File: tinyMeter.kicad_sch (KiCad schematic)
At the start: 30 parts, among them J1 USB_MASTER, J2 DC_POWER, J3 USB_POWER, J4 USBA_OUT_2, J5 USBA_OUT_1, J6 DC_POWER, Q1 BUK9832-55A, Q2 BUK9832-55A, Q3 BUK9832-55A, U1 ESP32-S3, U2 INA219AxD, U3 INA219AxD, U4 INA219AxD, U5 AMS1117-3.3

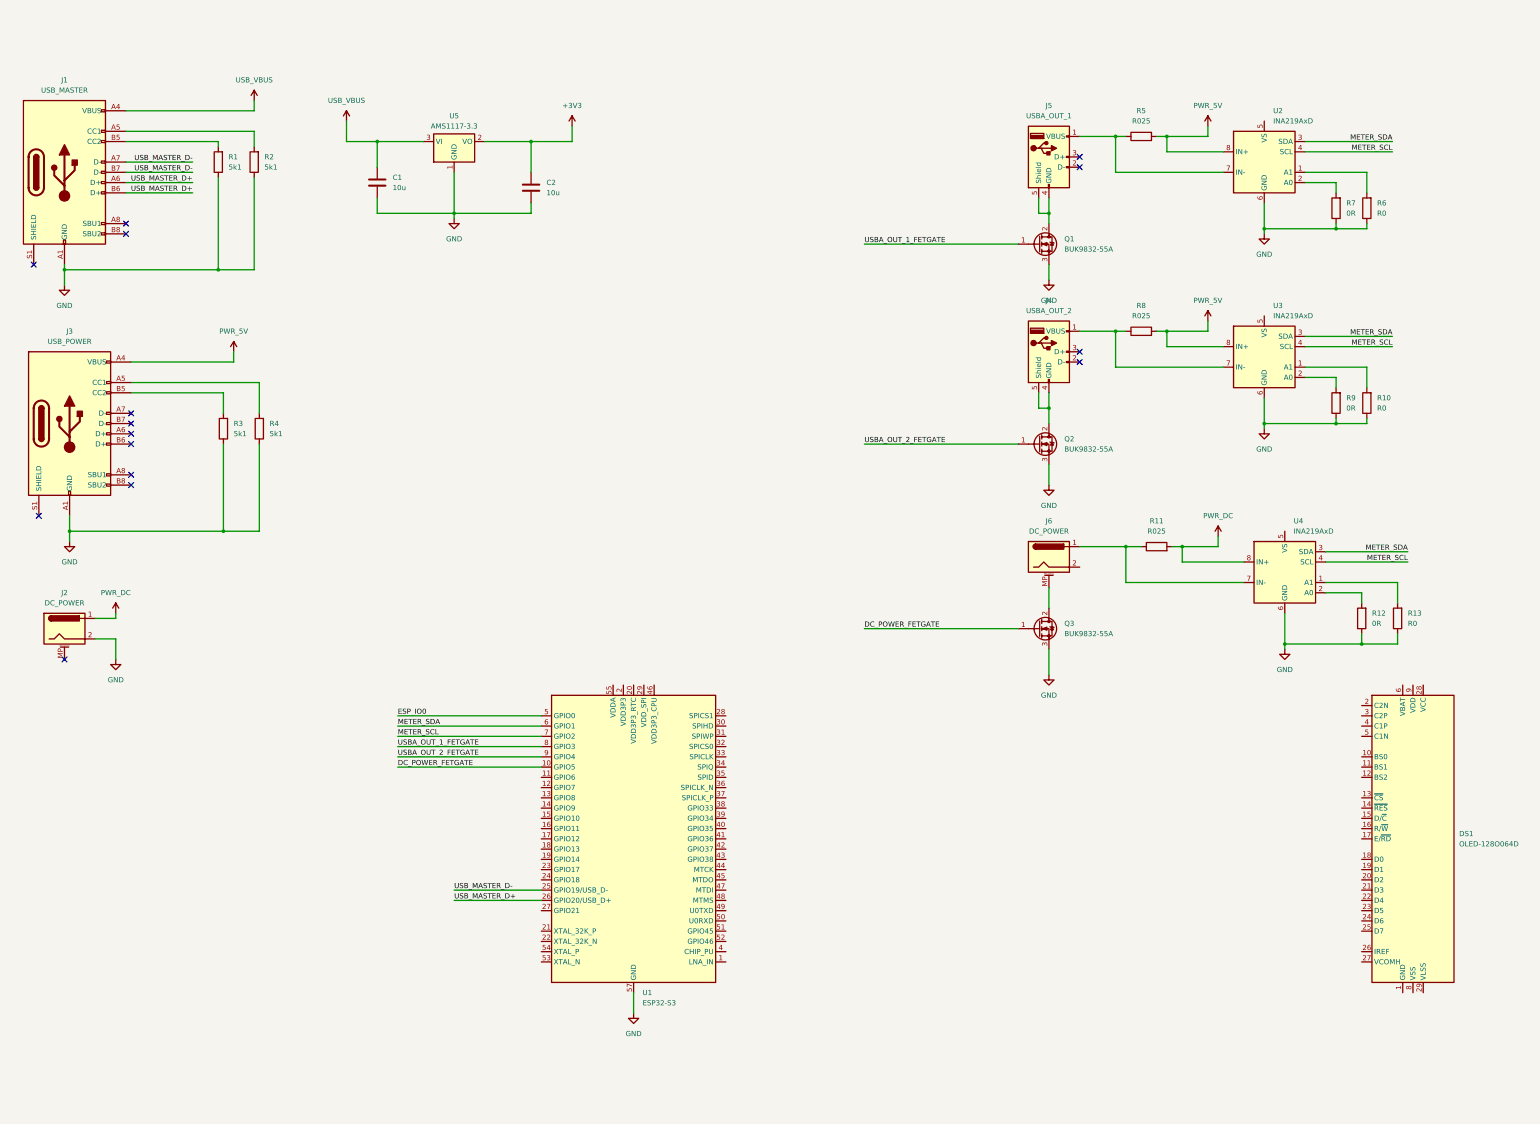
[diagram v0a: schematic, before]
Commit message: Rough schematic and start of layout
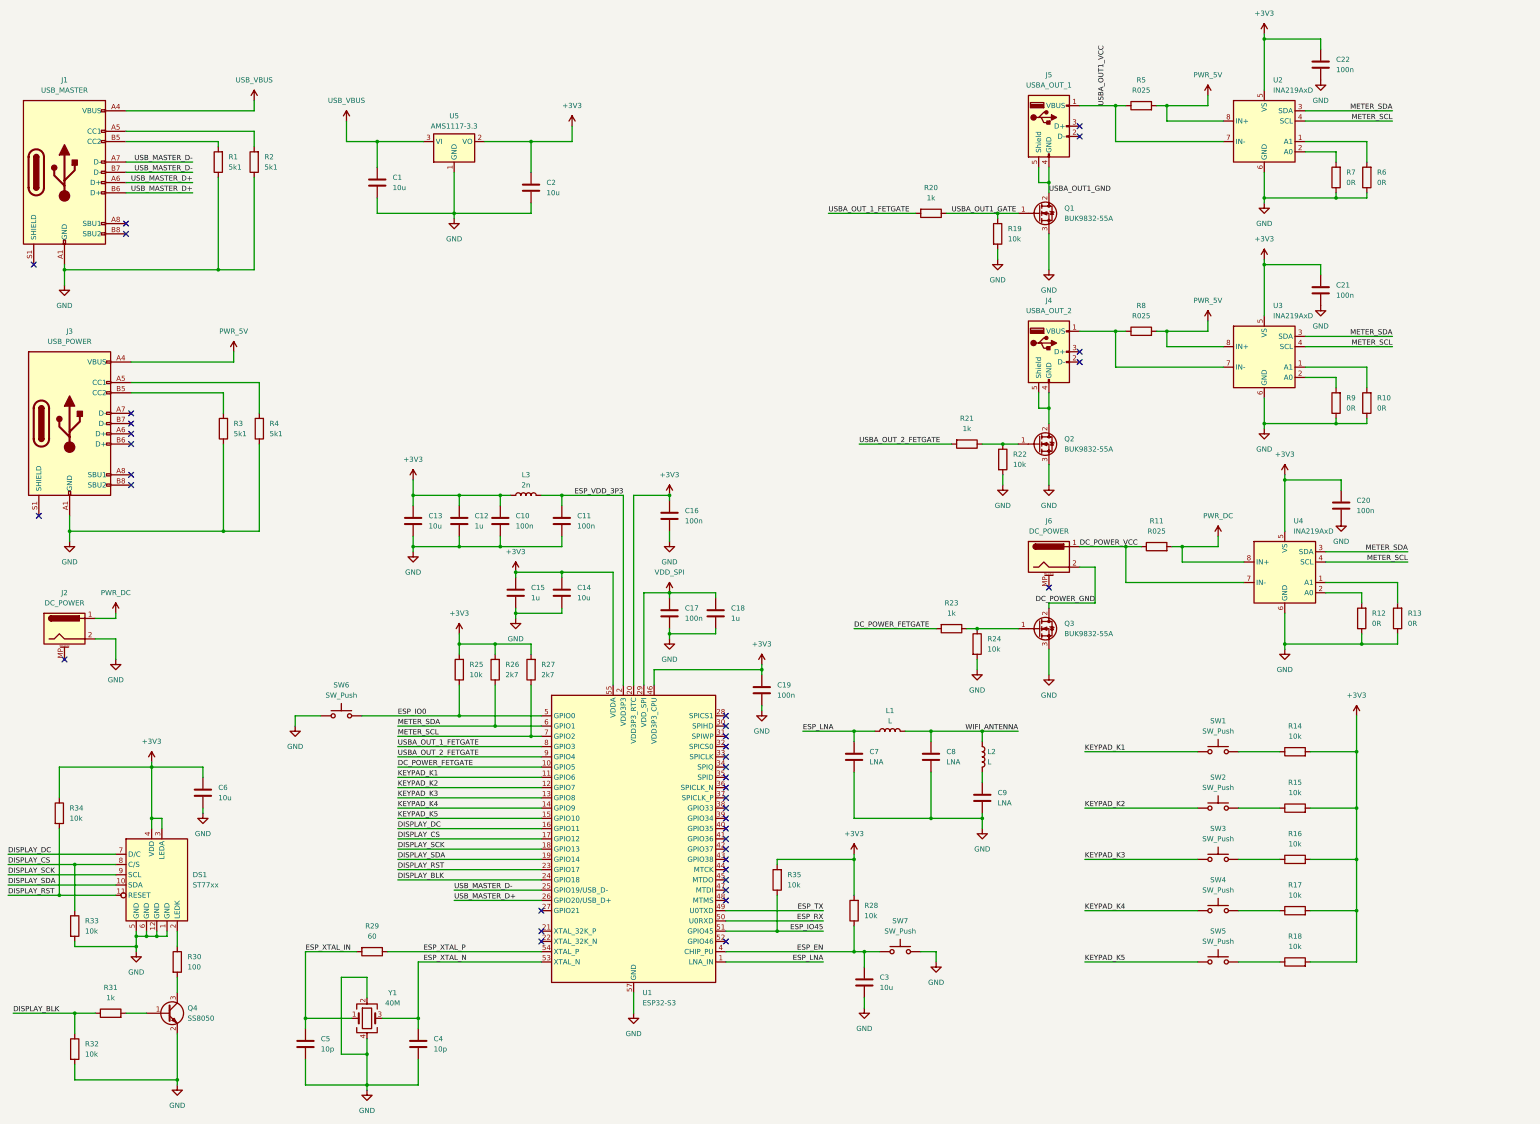
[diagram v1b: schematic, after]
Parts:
- removed DS1: OLED-128O064D, Display:OLED-128O064D, symbol Display_Graphic:OLED-128O064D
- added C10, C11, C16, C17, C19, C20, C21, C22: 100n, Capacitor_SMD:C_0603_1608Metric, symbol Device:C
- added C12, C15, C18: 1u, Capacitor_SMD:C_0603_1608Metric, symbol Device:C
- added C13, C14, C3, C6: 10u, Capacitor_SMD:C_0603_1608Metric, symbol Device:C
- added C4, C5: 10p, Capacitor_SMD:C_0603_1608Metric, symbol Device:C
- added C7, C8, C9: LNA, Capacitor_SMD:C_0603_1608Metric, symbol Device:C
- added DS1: ST77xx, Library:ST77XX, symbol Library:ST77xx
- added L1, L2: L, Capacitor_SMD:C_0603_1608Metric, symbol Device:L
- added L3: 2n, Capacitor_SMD:C_0603_1608Metric, symbol Device:L
- added Q4: SS8050, Package_TO_SOT_SMD:SOT-23, symbol Transistor_BJT:SS8050
- added R14, R15, R16, R17, R18, R19, R22, R24, R25, R28, R32, R33, R34, R35: 10k, Capacitor_SMD:C_0603_1608Metric, symbol Device:R
- added R20, R21, R23, R31: 1k, Capacitor_SMD:C_0603_1608Metric, symbol Device:R
- added R26, R27: 2k7, Capacitor_SMD:C_0603_1608Metric, symbol Device:R
- added R29: 60, Capacitor_SMD:C_0603_1608Metric, symbol Device:R
- added R30: 100, Capacitor_SMD:C_0603_1608Metric, symbol Device:R
- added SW1, SW2, SW3, SW4, SW5, SW6, SW7: SW_Push, Button_Switch_SMD:SW_SPST_B3U-1000P, symbol Switch:SW_Push
- added Y1: 40M, Crystal:Crystal_SMD_2016-4Pin_2.0x1.6mm, symbol Device:Crystal_GND24
- C1, C2: footprint (none) -> Capacitor_SMD:C_0805_2012Metric
- J1, J3: footprint (none) -> Connector_USB:USB_C_Receptacle_GCT_USB4105-xx-A_16P_TopMnt_Horizontal
- R1, R12, R2, R3, R4, R7, R9: footprint (none) -> Capacitor_SMD:C_0603_1608Metric
- R10, R13, R6: value R0 -> 0R; footprint (none) -> Capacitor_SMD:C_0603_1608Metric
- R11, R5, R8: footprint (none) -> Diode_SMD:D_2512_6332Metric
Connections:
- net +3V3: now also U1.20 (VDD3P3_RTC), U1.46 (VDD3P3_CPU), U1.55 (VDDA), U1.56 (VDDA), U2.5 (VS), U3.5 (VS), U4.5 (VS), C10.1, C12.1, C13.1, C14.1, C15.1, C16.1, C19.1, C20.1, C21.1, C22.1, C6.1, DS1.3 (LEDA), DS1.4 (VDD), L3.1, R14.2, R15.2, R16.2, R17.2, R18.2, R25.2, R26.2, R27.2, R28.2, R34.1, R35.2
- net DC_POWER_FETGATE: now also R23.2; no longer Q3.1 (G)
- net ESP_IO0: now also R25.1, SW6.2
- net GND: now also C10.2, C11.2, C12.2, C13.2, C14.2, C15.2, C16.2, C17.2, C18.2, C19.2, C20.2, C21.2, C22.2, C3.2, C4.2, C5.2, C6.2, C7.2, C8.2, C9.2, DS1.1 (GND), DS1.12 (GND), DS1.5 (GND), DS1.6 (GND), Q4.2 (E), R19.2, R22.2, R24.2, R32.2, R33.2, SW6.1, SW7.2, Y1.2, Y1.4
- net METER_SCL: now also R27.1
- net METER_SDA: now also R26.1
- net USBA_OUT_1_FETGATE: now also R20.2; no longer Q1.1 (G)
- net USBA_OUT_2_FETGATE: now also R21.2; no longer Q2.1 (G)
- net DC_POWER_VCC: now reaches J6.1, R11.1, U4.7 (IN-)
- net ESP_LNA: now reaches U1.1 (LNA_IN)
- net ESP_LNA: now also C7.1, L1.1
- net KEYPAD_K1: now reaches U1.11 (GPIO6)
- net KEYPAD_K1: now also SW1.1
- net KEYPAD_K2: now reaches U1.12 (GPIO7)
- net KEYPAD_K2: now also SW2.1
- net KEYPAD_K3: now reaches U1.13 (GPIO8)
- net KEYPAD_K3: now also SW3.1
- net KEYPAD_K4: now reaches U1.14 (GPIO9)
- net KEYPAD_K4: now also SW4.1
- net KEYPAD_K5: now reaches U1.15 (GPIO10)
- net KEYPAD_K5: now also SW5.1
- net DISPLAY_DC: now reaches U1.16 (GPIO11)
- net DISPLAY_DC: now also DS1.7 (D/C)
- net DISPLAY_CS: now reaches U1.17 (GPIO12)
- net DISPLAY_CS: now also DS1.8 (C/S), R33.1
- net DISPLAY_SCK: now reaches U1.18 (GPIO13)
- net DISPLAY_SCK: now also DS1.9 (SCL)
- net DISPLAY_SDA: now reaches U1.19 (GPIO14)
- net DISPLAY_SDA: now also DS1.10 (SDA)
- net ESP_VDD_3P3: now reaches U1.2 (VDD3P3), U1.3 (VDD3P3)
- net ESP_VDD_3P3: now also C11.1, L3.2
- net DISPLAY_RST: now reaches U1.23 (GPIO17)
- net DISPLAY_RST: now also DS1.11 (RESET), R34.2
- net DISPLAY_BLK: now reaches U1.24 (GPIO18)
- net DISPLAY_BLK: now also R31.1, R32.1
- net VDD_SPI: now reaches U1.29 (VDD_SPI)
- net VDD_SPI: now also C17.1, C18.1
- net ESP_EN: now reaches U1.4 (CHIP_PU)
- net ESP_EN: now also C3.1, R28.1, SW7.1
- net ESP_TX: now reaches U1.49 (U0TXD)
- net ESP_RX: now reaches U1.50 (U0RXD)
- net ESP_IO45: now reaches U1.51 (GPIO45)
- net ESP_IO45: now also R35.1
- net ESP_XTAL_N: now reaches U1.53 (XTAL_N)
- net ESP_XTAL_N: now also C4.1, Y1.3
- net ESP_XTAL_P: now reaches U1.54 (XTAL_P)
- net ESP_XTAL_P: now also R29.1
- net DC_POWER_GND: now reaches J6.2
- net DC_POWER_GND: now also Q3.2 (D)
- net at J6.MP (MountPin): no longer Q3.2 (D)
- net USBA_OUT1_GND: now reaches J5.4 (GND), J5.5 (Shield), Q1.2 (D)
- net USBA_OUT1_VCC: now reaches J5.1 (VBUS), R5.1, U2.7 (IN-)
- new net: Q3.1 (G), R23.1, R24.1
- new net: DS1.2 (LEDK), R30.1
- new net: R15.1, SW2.2
- new net: Q2.1 (G), R21.1, R22.1
- new net: R16.1, SW3.2
- new net: R17.1, SW4.2
- new net: Q4.1 (B), R31.2
- new net: R14.1, SW1.2
- new net: R18.1, SW5.2
- new net: C9.1, L2.2
- new net: Q4.3 (C), R30.2
- new net ESP_XTAL_IN: C5.1, R29.2, Y1.1
- new net USBA_OUT1_GATE: Q1.1 (G), R19.1, R20.1
- new net WIFI_ANTENNA: C8.1, L1.2, L2.1
- no-connect marks 15 -> 39
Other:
- moved on the sheet: J5, Q1, R5, R6, R7, U2

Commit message: Rough layout and routing
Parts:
- removed R10, R12, R13, R6, R7, R9: 0R, Capacitor_SMD:C_0603_1608Metric, symbol Device:R
- removed R35: 10k, Capacitor_SMD:C_0603_1608Metric, symbol Device:R
- added AE1: Antenna_Loop, Library:ESPRESSIF_ESP32_MIFA_2.4GHz_Right, symbol Device:Antenna_Loop
- added H1: 1, MountingHole:MountingHole_2.7mm_M2.5_DIN965_Pad, symbol Mechanical:MountingHole_Pad
- added H2: 2, MountingHole:MountingHole_2.7mm_M2.5_DIN965_Pad, symbol Mechanical:MountingHole_Pad
- added H3: 3, MountingHole:MountingHole_2.7mm_M2.5_DIN965_Pad, symbol Mechanical:MountingHole_Pad
- added H4: 4, MountingHole:MountingHole_2.7mm_M2.5_DIN965_Pad, symbol Mechanical:MountingHole_Pad
- Q1, Q2, Q3: value BUK9832-55A -> 100N03A; footprint Package_TO_SOT_SMD:SOT-223-3_TabPin2 -> Package_TO_SOT_SMD:TO-252-2
- R1, R14, R15, R16, R17, R18, R19, R2, R20, R21, R22, R23, R24, R25, R26, R27, R28, R29, R3, R30, R31, R32, R33, R34, R4: footprint Capacitor_SMD:C_0603_1608Metric -> Resistor_SMD:R_0603_1608Metric
- R11, R5, R8: footprint Diode_SMD:D_2512_6332Metric -> Resistor_SMD:R_2512_6332Metric
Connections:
- net +3V3: now also U3.1 (A1), U4.2 (A0)
- net DC_POWER_FETGATE: now also U1.42 (GPIO37); no longer U1.10 (GPIO5)
- net DC_POWER_VCC: now also U4.8 (IN+); no longer U4.7 (IN-)
- net DISPLAY_BLK: now also U1.6 (GPIO1); no longer U1.24 (GPIO18)
- net DISPLAY_CS: now also U1.8 (GPIO3); no longer U1.17 (GPIO12)
- net DISPLAY_DC: now also U1.7 (GPIO2); no longer U1.16 (GPIO11)
- net DISPLAY_RST: now also U1.11 (GPIO6); no longer U1.23 (GPIO17)
- net DISPLAY_SCK: now also U1.9 (GPIO4); no longer U1.18 (GPIO13)
- net DISPLAY_SDA: now also U1.10 (GPIO5); no longer U1.19 (GPIO14)
- net GND: now also U2.1 (A1), U2.2 (A0), U3.2 (A0), U4.1 (A1), AE1.2, H1.1, H2.1, H3.1, H4.1
- net KEYPAD_K1: now also U1.16 (GPIO11); no longer U1.11 (GPIO6)
- net KEYPAD_K2: now also U1.15 (GPIO10); no longer U1.12 (GPIO7)
- net KEYPAD_K3: now also U1.14 (GPIO9); no longer U1.13 (GPIO8)
- net KEYPAD_K4: now also U1.12 (GPIO7); no longer U1.14 (GPIO9)
- net KEYPAD_K5: now also U1.13 (GPIO8); no longer U1.15 (GPIO10)
- net METER_SCL: now also U1.39 (GPIO34); no longer U1.7 (GPIO2)
- net METER_SDA: now also U1.38 (GPIO33); no longer U1.6 (GPIO1)
- net PWR_5V: now also U2.7 (IN-), U3.7 (IN-); no longer U2.8 (IN+), U3.8 (IN+)
- net PWR_DC: now also U4.7 (IN-); no longer U4.8 (IN+)
- net USBA_OUT1_VCC: now also U2.8 (IN+); no longer U2.7 (IN-)
- net USBA_OUT_1_FETGATE: now also U1.40 (GPIO35); no longer U1.8 (GPIO3)
- net USBA_OUT_2_FETGATE: now also U1.41 (GPIO36); no longer U1.9 (GPIO4)
- net WIFI_ANTENNA: now also AE1.1
- net USBA_OUT2_VCC: now reaches J4.1 (VBUS), R8.1
- net USBA_OUT2_VCC: now also U3.8 (IN+); no longer U3.7 (IN-)
- net USBA_OUT2_GND: now reaches J4.4 (GND), J4.5 (Shield), Q2.2 (D)
- no-connect marks 39 -> 34
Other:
- moved on the sheet: R26, R27

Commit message: More layout
- Some traces refactor
- Add debug connector with UART lines
- Add external WiFi/BT connector and selector for PCB/Ext
- Add WS8212B LED just for fun
- Add power indication LED on 3V3
- Remove RefDes silkscreen; add useful silkscreen
- Add crystal 3D model
- Move display FPC connector to back side of the PCB; reroute display traces
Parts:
- added C23: 100n, Capacitor_SMD:C_0603_1608Metric, symbol Device:C
- added D1: WS2812B, LED_SMD:LED_WS2812B_PLCC4_5.0x5.0mm_P3.2mm, symbol LED:WS2812B
- added D2: PWR_LED, LED_SMD:LED_0603_1608Metric, symbol PCM_SL_Devices:LED
- added J7: Debug, Connector_PinSocket_2.54mm:PinSocket_1x04_P2.54mm_Horizontal, symbol Connector_Generic:Conn_01x04
- added J8: External antenna, Connector_Coaxial:U.FL_Hirose_U.FL-R-SMT-1_Vertical, symbol Connector:Conn_Coaxial
- added R10, R6, R7, R9: 0R, Resistor_SMD:R_0603_1608Metric, symbol Device:R
- added R12, R13: 220, Resistor_SMD:R_0603_1608Metric, symbol Device:R
- AE1: value Antenna_Loop -> PCB antenna
- L1, L2, L3: footprint Capacitor_SMD:C_0603_1608Metric -> Inductor_SMD:L_0603_1608Metric
- Y1: value 40M -> Crystal_GND24; footprint Crystal:Crystal_SMD_2016-4Pin_2.0x1.6mm -> Library:OSC_XRCGB40M000F4M00R0
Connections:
- net +3V3: now also J7.2 (Pin_2), R13.1
- net DISPLAY_BLK: now also U1.11 (GPIO6); no longer U1.6 (GPIO1)
- net DISPLAY_CS: now also U1.9 (GPIO4); no longer U1.8 (GPIO3)
- net DISPLAY_DC: now also U1.10 (GPIO5); no longer U1.7 (GPIO2)
- net DISPLAY_RST: now also U1.6 (GPIO1); no longer U1.11 (GPIO6)
- net DISPLAY_SCK: now also U1.8 (GPIO3); no longer U1.9 (GPIO4)
- net DISPLAY_SDA: now also U1.7 (GPIO2); no longer U1.10 (GPIO5)
- net ESP_RX: now also J7.4 (Pin_4), R7.1; no longer U1.50 (U0RXD)
- net ESP_TX: now also J7.3 (Pin_3), R6.1; no longer U1.49 (U0TXD)
- net GND: now also C23.2, D1.3 (VSS), D2.1, J7.1 (Pin_1), J8.2 (Ext)
- net USB_VBUS: now also C23.1, D1.1 (VDD)
- net WIFI_ANTENNA: now also R10.1, R9.1; no longer AE1.1
- net MCU_LED_DATA: now reaches U1.17 (GPIO12)
- net MCU_LED_DATA: now also R12.2
- new net: D2.2, R13.2
- new net: J8.1 (In), R10.2
- new net: R6.2, U1.49 (U0TXD)
- new net: R7.2, U1.50 (U0RXD)
- new net: D1.4 (DIN), R12.1
- new net: AE1.1, R9.2
- no-connect marks 34 -> 35
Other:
- moved on the sheet: H1, H2, H3, H4

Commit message: Fixes and schematic refactor
- Refactor schematic to get more space
- Assign nets where missing
- Change footprint of USB-C
- Add 3D model for USB-C footprint
- Changes to board setup
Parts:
- J1, J3: footprint Connector_USB:USB_C_Receptacle_GCT_USB4105-xx-A_16P_TopMnt_Horizontal -> Connector_USB:USB_C_Receptacle_HRO_TYPE-C-31-M-12
- SW6: value SW_Push -> Boot
- SW7: value SW_Push -> Reset
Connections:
- net DC_POWER_GATE: now reaches Q3.1 (G), R23.1, R24.1
- net DISPLAY_LEDK: now reaches DS1.2 (LEDK), R30.1
- net 3V3_PWR_LED: now reaches D2.2, R13.2
- net WIFI_ANTENNA_EXT: now reaches J8.1 (In), R10.2
- net USBA_OUT2_GATE: now reaches Q2.1 (G), R21.1, R22.1
- net USB_POWER_CC1: now reaches J3.A5 (CC1), R4.2
- net ESP_TDX0: now reaches R6.2, U1.49 (U0TXD)
- net ESP_RDX0: now reaches R7.2, U1.50 (U0RXD)
- net MCU_LED_DIN: now reaches D1.4 (DIN), R12.1
- net DISPLAY_BLK_GATE: now reaches Q4.1 (B), R31.2
- net USB_POWER_CC2: now reaches J3.B5 (CC2), R3.2
- net USB_MASTER_CC2: now reaches J1.B5 (CC2), R1.2
- net WIFI_ANTENNA_F: now reaches C9.1, L2.2
- net WIFI_ANTENNA_PCB: now reaches AE1.1, R9.2
- net USB_MASTER_CC1: now reaches J1.A5 (CC1), R2.2
- net DISPLAY_LEDK_R: now reaches Q4.3 (C), R30.2
- no-connect marks 35 -> 39
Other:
- moved on the sheet: AE1, C1, C10, C11, C12, C13, C14, C15, C16, C17, C18, C19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

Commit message: Fix display connector orientation
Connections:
- net DISPLAY_BLK: now also U1.6 (GPIO1); no longer U1.11 (GPIO6)
- net DISPLAY_CS: now also U1.8 (GPIO3); no longer U1.9 (GPIO4)
- net DISPLAY_DC: now also U1.7 (GPIO2); no longer U1.10 (GPIO5)
- net DISPLAY_RST: now also U1.11 (GPIO6); no longer U1.6 (GPIO1)
- net DISPLAY_SCK: now also U1.9 (GPIO4); no longer U1.8 (GPIO3)
- net DISPLAY_SDA: now also U1.10 (GPIO5); no longer U1.7 (GPIO2)
- net METER_SCL: now also R26.1, U1.40 (GPIO35); no longer R27.1, U1.39 (GPIO34)
- net METER_SDA: now also R27.1, U1.39 (GPIO34); no longer R26.1, U1.38 (GPIO33)
- net USBA_OUT_1_FETGATE: now also U1.38 (GPIO33); no longer U1.40 (GPIO35)
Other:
- moved on the sheet: AE1, C10, C11, C12, C13, C14, C15, C16, C17, C18, C19, C20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
